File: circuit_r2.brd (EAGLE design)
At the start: 20.4 x 52.1 mm, 16 parts, among them IC1 7805DT, U1 MCP4725, U2 MB85RC256VPF-G-JNERE2

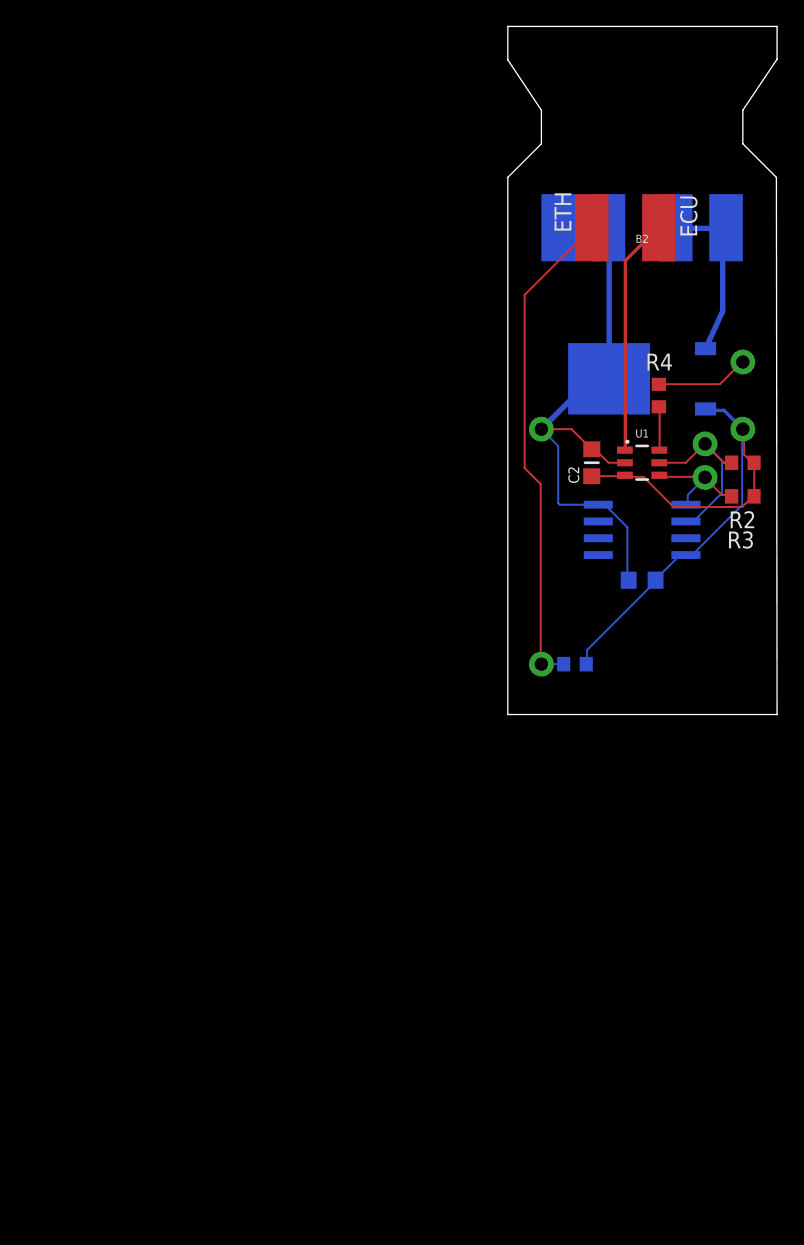
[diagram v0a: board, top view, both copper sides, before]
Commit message: Working on a version without the promini.
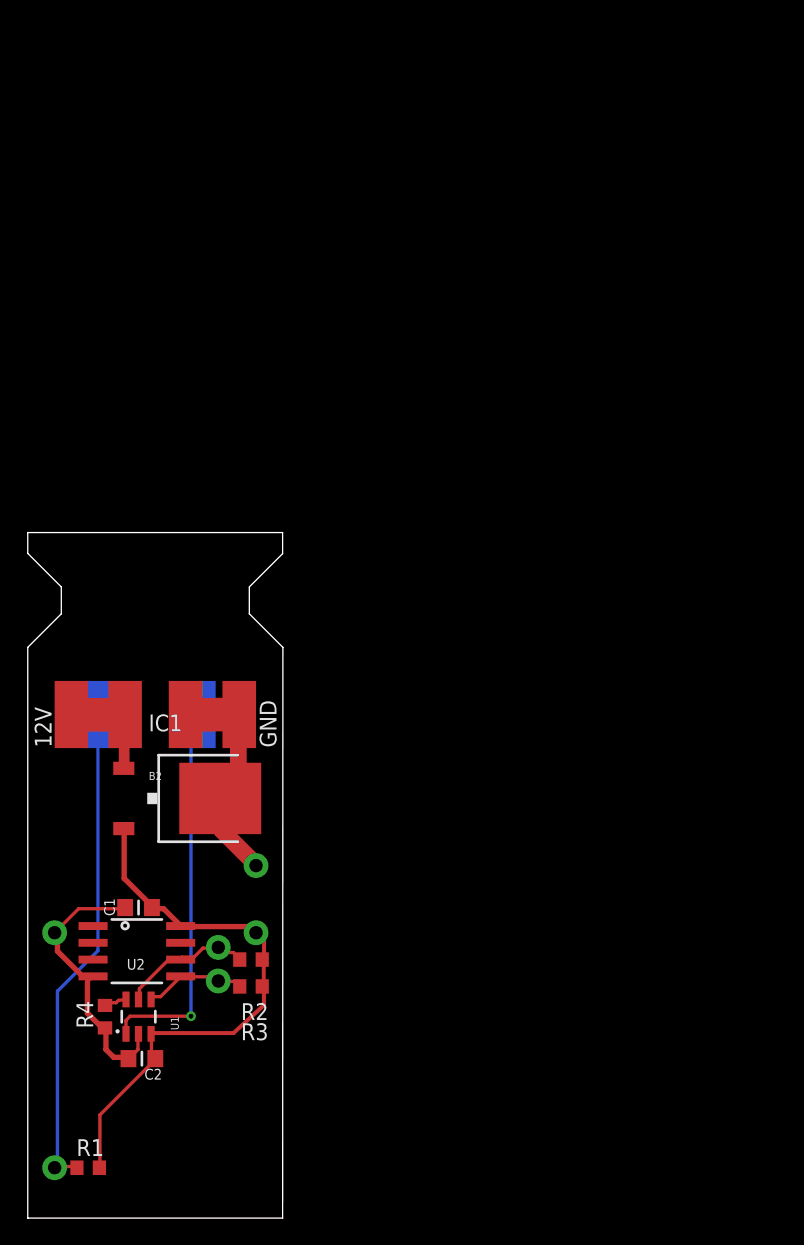
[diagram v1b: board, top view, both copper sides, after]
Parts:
- moved R4 63.0 mm to (6.35, 15.2), turned to 90 degrees
- moved 12V 61.7 mm to (3.81, 38.1), flipped to the top, turned to 0 degrees
- moved U1 56.6 mm to (8.89, 15.2), turned to 180 degrees
- moved C2 56.5 mm to (9.14, 12.1), turned to 180 degrees
- moved ETH_PWR 55.6 mm to (7.87, 38.1), flipped to the top, turned to 0 degrees
- moved B2 53.0 mm to (10.2, 16.5)
- moved R1 53.0 mm to (5.08, 3.81), flipped to the top, turned to 0 degrees
- moved R2 52.9 mm to (17.4, 19.6)
- moved R3 52.5 mm to (17.4, 17.5)
- moved ETH 52.4 mm to (5.97, 38.1), flipped to the bottom
- moved ECU 50.7 mm to (13.5, 38.1), flipped to the bottom, turned to 0 degrees
- moved U2 49.8 mm to (8.76, 20.2), flipped to the top, turned to 270 degrees
- moved ETH_GND 48.8 mm to (12.4, 38.1), flipped to the top, turned to 0 degrees
- moved IC1 46.8 mm to (12.6, 31.8), flipped to the top
- moved C1 45.4 mm to (8.89, 23.5), flipped to the top, turned to 180 degrees
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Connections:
- net N$4 renamed PD_L
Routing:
- net GND: track 53.0 -> 39.2 mm
- net OUT: track 17.9 -> 29.1 mm, vias 0 -> 1
- net VIN: track 13.2 -> 8.15 mm
- net SCL: track 14.5 -> 10.1 mm
- net VCC: track 45.9 -> 42.9 mm
- net PD_L: track 3.29 -> 1.81 mm
- net SDA: track 8.85 -> 8.17 mm
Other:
- board size 20.4 x 52.1 mm -> 19.3 x 51.9 mm
